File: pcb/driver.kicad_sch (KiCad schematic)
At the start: 5 parts, among them J10 Conn_01x05_Pin, J8 HallSensor, U5 ULN2003A

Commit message: S E N T
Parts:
- added R1, R7: 20k, Resistor_SMD:R_0805_2012Metric, symbol Device:R_Small_US
- J8: LCSC C144394 -> C6332196; now in the parts list
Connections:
- net GND: now also R7.2
- net OUT_HALL: now also R1.2, R7.1; no longer J8.3 (Pin_3)
- net +3V3 renamed +5V
- new net: J8.3 (Pin_3), R1.1

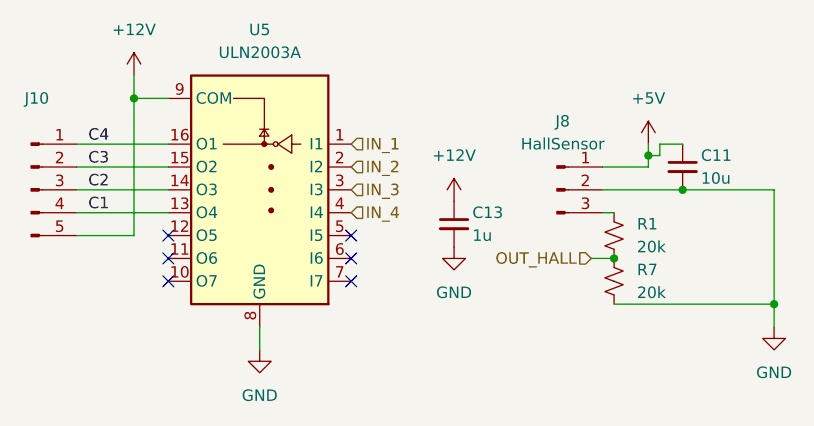
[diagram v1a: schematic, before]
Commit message: ordered ol
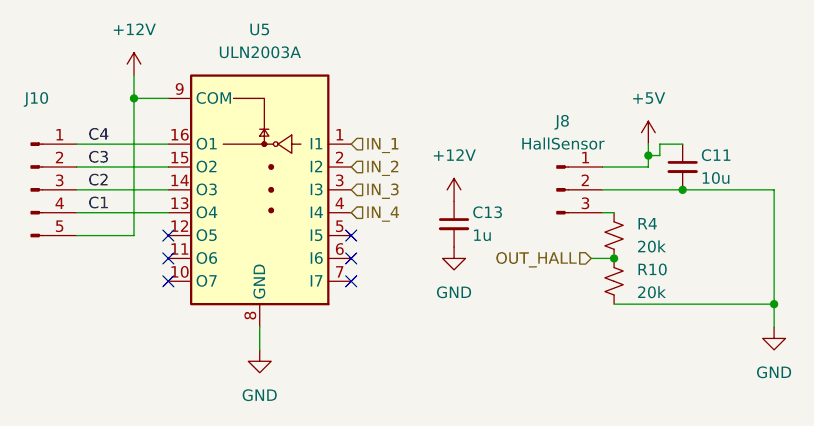
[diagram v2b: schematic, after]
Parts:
- renumbered R7 to R10, R1 to R4
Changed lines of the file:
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@@
 		(dnp no)
 		(fields_autoplaced yes)
-		(property "Reference" "R1"
+		(property "Reference" "R4"
 			(at 92.71 38.0999 0)
 			(effects
@@
 		(dnp no)
 		(fields_autoplaced yes)
-		(property "Reference" "#PWR03"
+		(property "Reference" "#PWR015"
 			(at 93.98 33.02 0)
 			(effects
@@
 		(dnp no)
 		(fields_autoplaced yes)
-		(property "Reference" "R7"
+		(property "Reference" "R10"
 			(at 92.71 43.1799 0)
 			(effects
